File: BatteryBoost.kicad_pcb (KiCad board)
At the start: 2 copper layers, 78 x 40 mm, 35 parts, among them J1 USB_B_Micro, J2 Conn_01x02, J3 Conn_01x02, J4 Mounting Hole, J5 Mounting Hole, J6 Mounting Hole, J7 Mounting Hole, Q1 Q_PMOS_GSD, SW1 SW_SPDT, U1 SP34063AEN, U2 TP4056

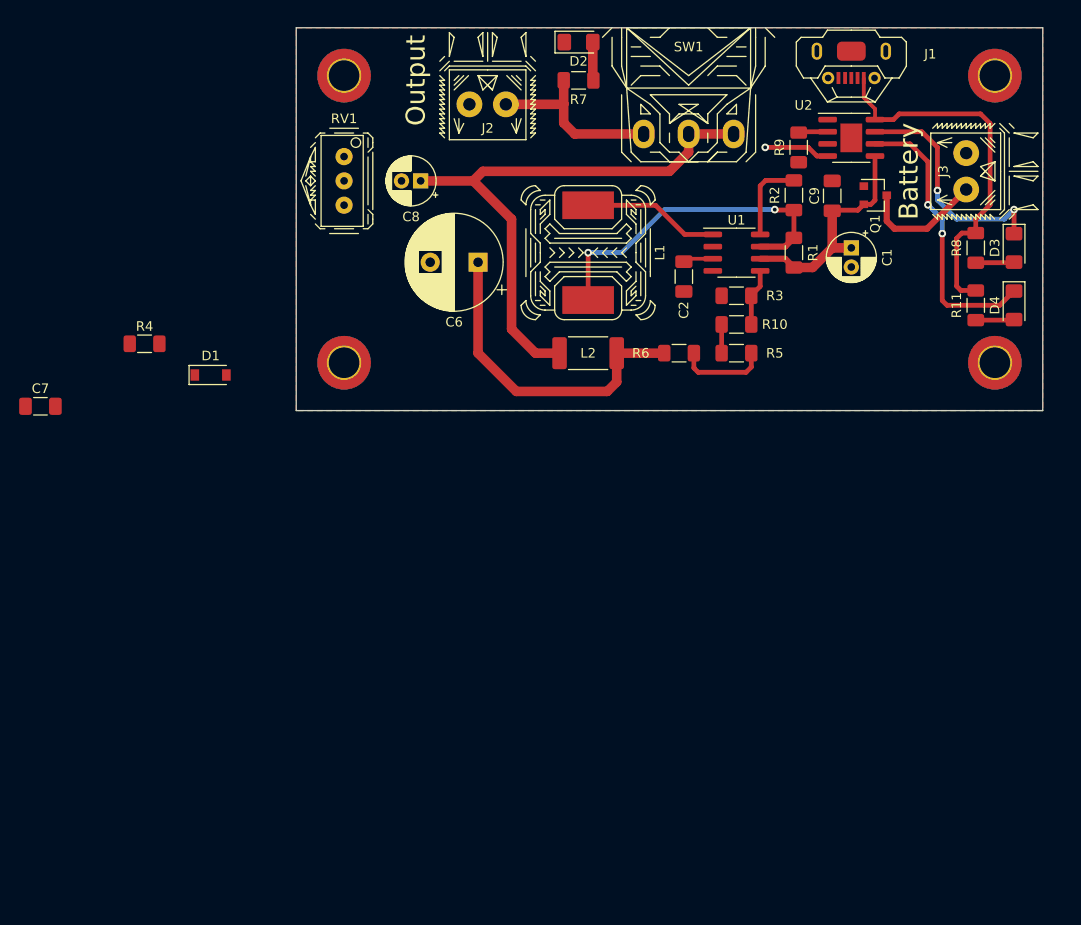
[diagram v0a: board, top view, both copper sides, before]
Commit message: add chamfer to board edge
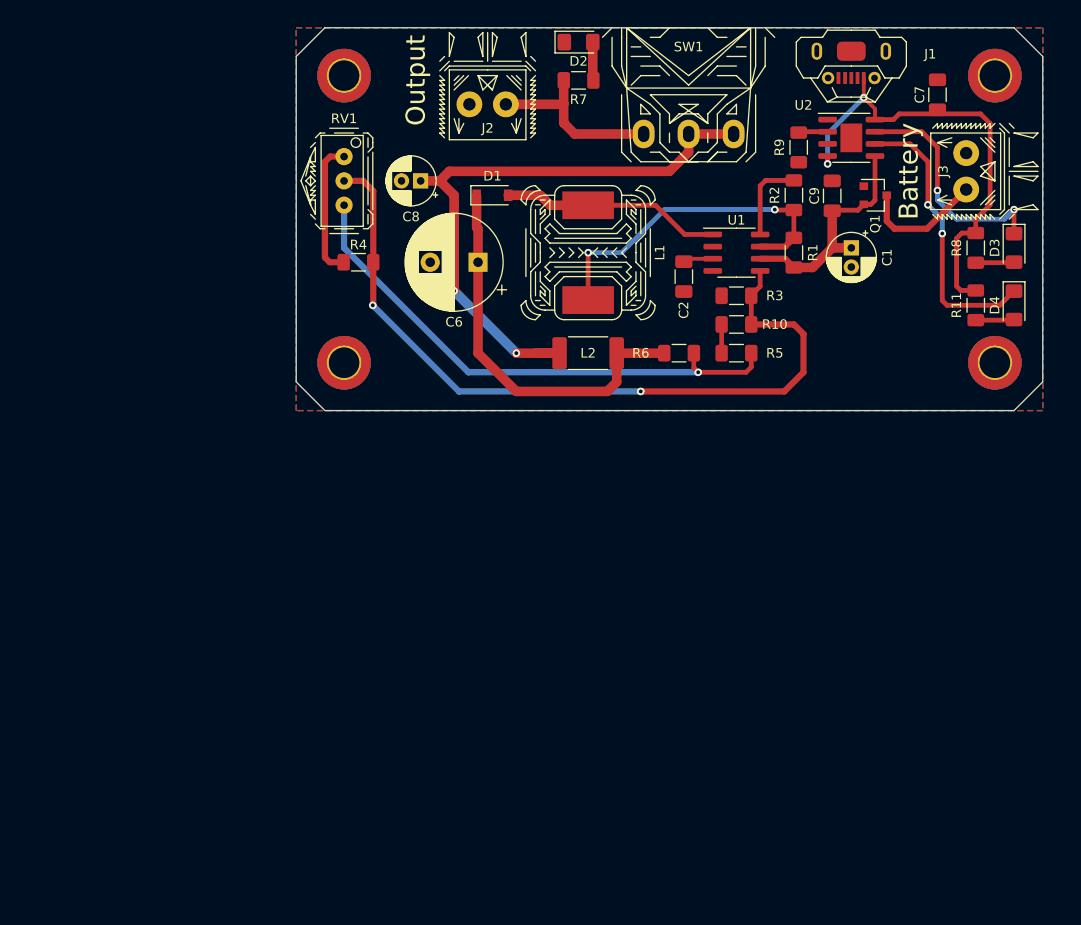
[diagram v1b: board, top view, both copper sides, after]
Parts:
- moved C7 99.2 mm to (67.0, 7.00), turned to 90 degrees
- moved D1 34.9 mm to (20.5, 17.5)
- moved R4 23.9 mm to (6.50, 24.5)
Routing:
- net Net-(R10-Pad2): track 5.98 -> 80.9 mm, vias 0 -> 2
- net Net-(R5-Pad1): track 9.41 -> 56.3 mm, vias 0 -> 1
- net Net-(R4-Pad1): track 0.00 -> 14.4 mm
- net Net-(D1-Pad2): track 14.3 -> 23.1 mm
- net Net-(C6-Pad1): track 34.1 -> 41.2 mm
- net +24V: track 59.0 -> 64.2 mm, vias 0 -> 2
- net +5V: track 45.9 -> 48.3 mm, vias 1 -> 2
- added copper zone on B.Cu, net GND
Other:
- outline, holes or cut-outs redrawn

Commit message: finalize designs
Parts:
- added D5: 40V 1A 450mV @ 1A, Diode_SMD:D_SOD-123, F.Cu at (58.0, 23.5)
- added D6: 40V 1A 450mV @ 1A, Diode_SMD:D_SOD-123, F.Cu at (55.0, 23.5)
- added G***: LOGO, BatteryBoost:F_Artwork, F.Cu at (40.0, 20.0)
- D1: value 40V 1A 450mV @ 1A -> 600V 5A 1.2V; footprint Diode_SMD:D_SOD-123 -> Diode_SMD:D_SMB
- L1: footprint BatteryBoost:Inductor_SLH_12x12x8 -> BatteryBoost:Inductor_SLH_12x12x8_HandSolder
- moved L2 20.9 mm to (42.2, 16.8)
- moved C1 4.91 mm to (62.8, 24.2), turned to 0 degrees
- moved D1 1.80 mm to (19.9, 15.8)
- moved J1 0.25 mm to (58.0, 5.00)
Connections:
- C1 pad 1: VBATT -> Net-(C1-Pad1)
- R1 pad 2: VBATT -> Net-(C1-Pad1)
- U1 pad 2: Net-(U1-Pad2) -> GND
- U1 pad 6: VBATT -> Net-(C1-Pad1)
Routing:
- net Net-(C6-Pad1): track 41.2 -> 67.2 mm, vias 0 -> 2
- net +24V: track 64.2 -> 40.9 mm, vias 2 -> 0
- net Net-(C1-Pad1): track 0.00 -> 15.1 mm
- net Net-(D1-Pad2): track 23.1 -> 9.63 mm
- net VBATT: track 24.2 -> 12.7 mm
- net +5V: track 48.3 -> 57.4 mm, vias 2 -> 3
- net Net-(R10-Pad2): track 80.9 -> 75.4 mm
- added copper zone on F.Cu, net Net-(D1-Pad2)
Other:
- board text removed: "Battery"
- board text removed: "Output"

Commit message: Finalize schematic and layout
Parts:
- removed D5, D6: 40V 1A 450mV @ 1A, Diode_SMD:D_SOD-123
- removed G***: LOGO, BatteryBoost:F_Artwork
- added Q2: Q_PMOS_GSD, Package_TO_SOT_SMD:SOT-23, F.Cu at (56.5, 23.8)
- added Q3: Q_PMOS_GSD, Package_TO_SOT_SMD:SOT-23, F.Cu at (62.0, 23.8)
- added R12: 1M, Resistor_SMD:R_1206_3216Metric_Pad1.30x1.75mm_HandSolder, F.Cu at (57.5, 35.5)
- added R14: 10k, Resistor_SMD:R_1206_3216Metric_Pad1.30x1.75mm_HandSolder, F.Cu at (64.8, 35.5)
- added U3: SN74LVC2G04DBVR, Package_TO_SOT_SMD:SOT-23-6, F.Cu at (61.0, 31.0)
- J2: value Conn_01x02 -> Output
- J3: value Conn_01x02 -> Battery
- Q1: footprint Package_TO_SOT_SMD:SC-59 -> Package_TO_SOT_SMD:SOT-23
- moved L2 13.4 mm to (29.5, 12.8)
- moved C1 8.40 mm to (55.0, 27.5), turned to 270 degrees
- moved R7 2.50 mm to (29.5, 8.00)
- moved D2 2.00 mm to (29.5, 3.50)
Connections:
- J2 pad 1: Net-(J2-Pad1) -> +24V
- R7 pad 1: Net-(J2-Pad1) -> +24V
- SW1 pad 1: Net-(J2-Pad1) -> Net-(C1-Pad1)
- SW1 pad 2: +24V -> SMPS_Pwr
- SW1 pad 3: +24V -> Net-(SW1-Pad3)
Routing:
- net VBATT: track 12.7 -> 50.3 mm, vias 0 -> 2
- net SMPS_Pwr: track 0.00 -> 31.0 mm, vias 0 -> 2
- net Net-(J2-Pad1): track 19.3 -> 0.00 mm
- net Net-(C1-Pad1): track 15.1 -> 31.9 mm
- net Net-(Q3-Pad1): track 0.00 -> 15.1 mm
- net +5V: track 57.4 -> 72.0 mm, vias 3 -> 4
- net +24V: track 40.9 -> 27.0 mm
- net Net-(C6-Pad1): track 67.2 -> 59.8 mm
- net GND: track 0.00 -> 6.04 mm, vias 0 -> 7
- net Net-(L1-Pad2): track 35.1 -> 34.5 mm
- net Net-(D2-Pad2): track 4.03 -> 4.53 mm

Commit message: A01 Release Files
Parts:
- removed the Q2 at (56.5, 23.8)
- added G***: LOGO, BatteryBoost:B_Artwork, B.Cu at (39.0, 20.0)
- added G***: LOGO, BatteryBoost:F_Artwork, F.Cu at (39.0, 20.0)
- added Q1: Q_PMOS_GSD, Package_TO_SOT_SMD:SOT-23, F.Cu at (56.5, 23.8)
- L2: value 1uH ±20% 3.29A 59mΩ SMD,2.5x2x1.2mm -> 1uH ±20% 3.29A 59mΩ
- R1: value 0.22 R -> 0.3R
- renumbered C7 to C2, C2 to C3, C6 to C4, C9 to C5, C8 to C6, D4 to D1, D1 to D2, D2 to D4, J4 to J1, J5 to J2, J6 to J3, J7 to J4, J1 to J5, J3 to J6, J2 to J7, Q1 to Q2, R12 to R10, R9 to R11, R7 to R12, R14 to R13, R10 to R3, R3 to R4, R11 to R5, R5 to R6, R4 to R7, R6 to R9
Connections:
- U2 pad 9: (no net) -> GND
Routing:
- net GND: track 6.04 -> 9.33 mm, vias 7 -> 8
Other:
- board text added: "JLCJLCJLCJLC"

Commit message: Clear board
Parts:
- removed C1, C6: 100uF ±20% 50V, Capacitor_THT:CP_Radial_D5.0mm_P2.00mm
- removed C2, C5: 10uF, Capacitor_SMD:C_1206_3216Metric_Pad1.33x1.80mm_HandSolder
- removed C3: 1.5nF ±10% 50V X7R 1206, Capacitor_SMD:C_1206_3216Metric_Pad1.33x1.80mm_HandSolder
- removed C4: 330uF ±20% 50V, Capacitor_THT:CP_Radial_D10.0mm_P5.00mm
- removed D1, D4: Blue LED, Diode_SMD:D_1206_3216Metric_Pad1.42x1.75mm_HandSolder
- removed D2: 600V 5A 1.2V, Diode_SMD:D_SMB
- removed D3: Red LED, Diode_SMD:D_1206_3216Metric_Pad1.42x1.75mm_HandSolder
- removed G***: LOGO, BatteryBoost:B_Artwork
- removed G***: LOGO, BatteryBoost:F_Artwork
- removed J5: USB_B_Micro, BatteryBoost:U-F-M5DD-Y-L
- removed J6: Battery, BatteryBoost:WJ124-3.81-2P
- removed J7: Output, BatteryBoost:WJ124-3.81-2P
- removed L1: 150uH ±20% 1.42A 280mΩ, BatteryBoost:Inductor_SLH_12x12x8_HandSolder
- removed L2: 1uH ±20% 3.29A 59mΩ, Inductor_SMD:L_2512_6332Metric_Pad1.52x3.35mm_HandSolder
- removed Q1, Q2, Q3: Q_PMOS_GSD, Package_TO_SOT_SMD:SOT-23
- removed R1: 0.3R, Resistor_SMD:R_1206_3216Metric_Pad1.30x1.75mm_HandSolder
- removed R10: 1M, Resistor_SMD:R_1206_3216Metric_Pad1.30x1.75mm_HandSolder
- removed R11: 1.2 k, Resistor_SMD:R_1206_3216Metric_Pad1.30x1.75mm_HandSolder
- removed R12, R13, R5, R8: 10k, Resistor_SMD:R_1206_3216Metric_Pad1.30x1.75mm_HandSolder
- removed R2: 180R, Resistor_SMD:R_1206_3216Metric_Pad1.30x1.75mm_HandSolder
- removed R3: 499k 0.25W 1%, Resistor_SMD:R_1206_3216Metric_Pad1.30x1.75mm_HandSolder
- removed R4: 16k, Resistor_SMD:R_1206_3216Metric_Pad1.30x1.75mm_HandSolder
- removed R6: 9.1k 1% 0.25W, Resistor_SMD:R_1206_3216Metric_Pad1.30x1.75mm_HandSolder
- removed R7: 0R, Resistor_SMD:R_1206_3216Metric_Pad1.30x1.75mm_HandSolder
- removed R9: 48k, Resistor_SMD:R_1206_3216Metric_Pad1.30x1.75mm_HandSolder
- removed RV1: 500k, BatteryBoost:Potentiometer_3296W-1-504
- removed SW1: SW_SPDT, BatteryBoost:Switch_SS-12D06L5
- removed U1: SP34063AEN, Package_SO:SOIC-8_3.9x4.9mm_P1.27mm
- removed U2: TP4056, BatteryBoost:SOIC-8-1EP_3.9x4.9mm_P1.27mm_EP2.29x3mm
- removed U3: SN74LVC2G04DBVR, Package_TO_SOT_SMD:SOT-23-6
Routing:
- net Net-(R3-Pad2): track 75.4 -> 0.00 mm, vias 2 -> 0
- net +5V: track 72.0 -> 0.00 mm, vias 4 -> 0
- net Net-(C4-Pad1): track 59.8 -> 0.00 mm, vias 2 -> 0
- net Net-(R6-Pad1): track 56.3 -> 0.00 mm, vias 1 -> 0
- net VBATT: track 50.3 -> 0.00 mm, vias 2 -> 0
- net Net-(L1-Pad2): track 34.5 -> 0.00 mm, vias 2 -> 0
- net Net-(C1-Pad1): track 31.9 -> 0.00 mm
- net SMPS_Pwr: track 31.0 -> 0.00 mm, vias 2 -> 0
- net Net-(D1-Pad1): track 29.7 -> 0.00 mm, vias 2 -> 0
- net +24V: track 27.0 -> 0.00 mm
- net Net-(D3-Pad1): track 24.5 -> 0.00 mm, vias 2 -> 0
- net Net-(Q3-Pad1): track 15.1 -> 0.00 mm
- net Net-(R7-Pad1): track 14.4 -> 0.00 mm
- net Net-(J6-Pad1): track 13.1 -> 0.00 mm
- net Net-(D2-Pad2): track 9.63 -> 0.00 mm
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- removed copper zone on F.Cu, net Net-(D2-Pad2)
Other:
- board text removed: "JLCJLCJLCJLC"

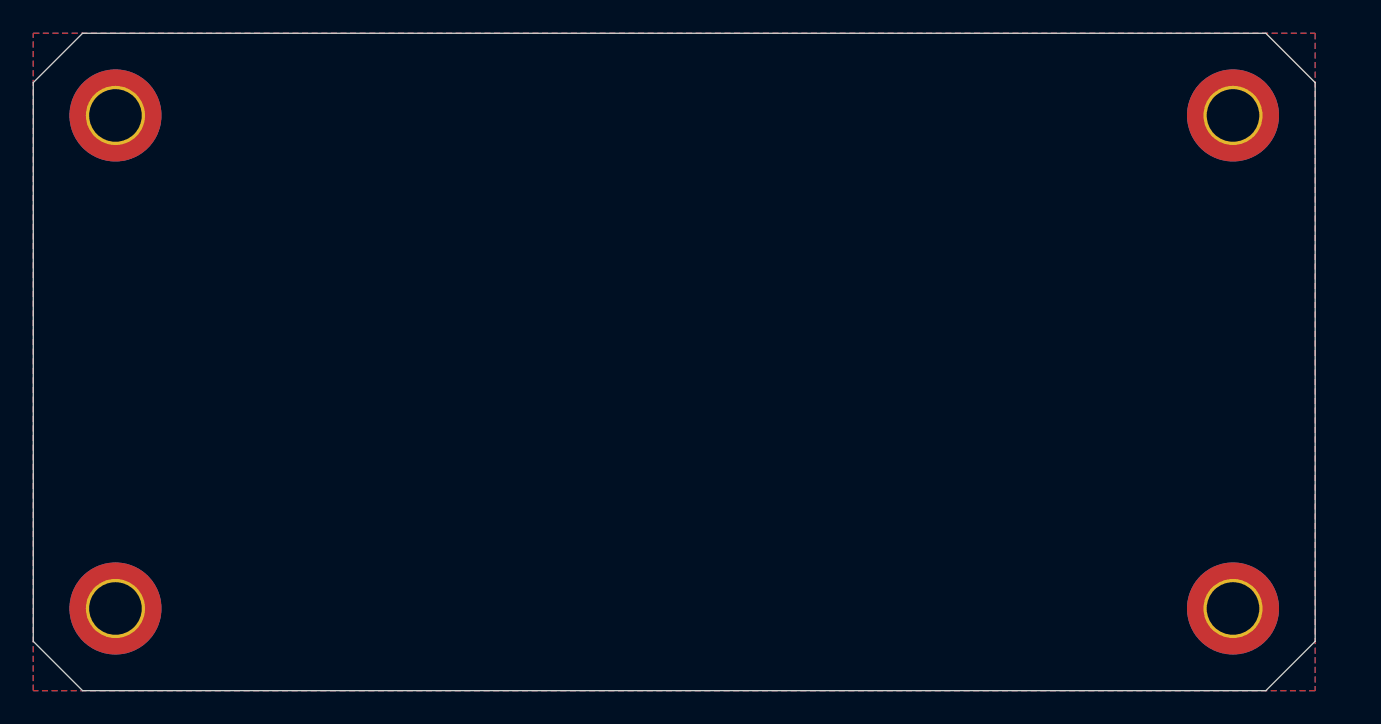
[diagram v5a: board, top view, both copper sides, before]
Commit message: update board size to 80x40mm
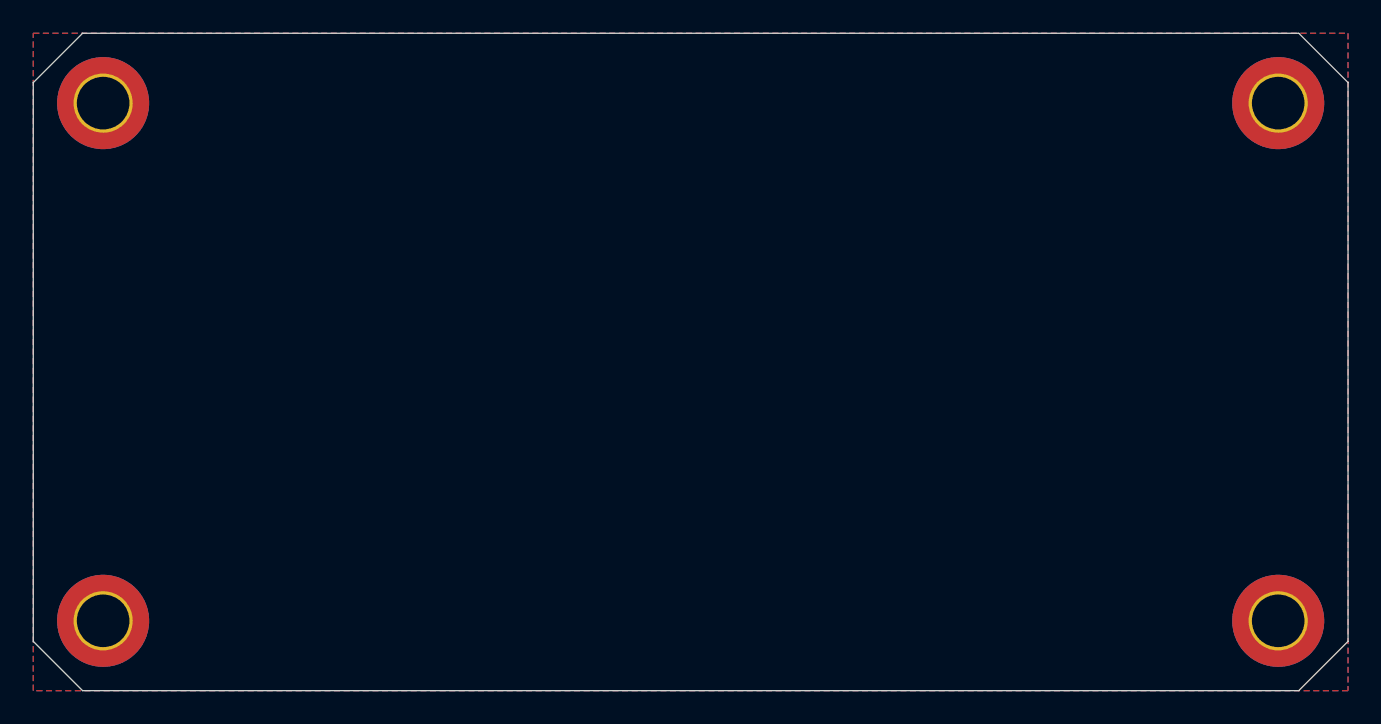
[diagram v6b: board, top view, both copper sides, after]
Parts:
- moved J2 2.85 mm to (75.8, 35.8)
- moved J3 2.85 mm to (75.8, 4.25)
- moved J1 1.06 mm to (4.25, 4.25)
- moved J4 1.06 mm to (4.25, 35.8)
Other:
- board size 78 x 40 mm -> 80 x 40 mm
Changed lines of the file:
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@@
   (general
     (thickness 1.6)
-    (drawings 8)
+    (drawings 12)
     (tracks 0)
     (zones 0)
@@
   )
   (module MountingHole:MountingHole_3.2mm_M3_DIN965_Pad_TopBottom locked (layer F.Cu)
-    (at 5 35)
+    (at 4.25 35.75)
     (descr "Mounting Hole 3.2mm, M3, DIN965")
     (tags "mounting hole 3.2mm m3 din965")
@@
   )
   (module MountingHole:MountingHole_3.2mm_M3_DIN965_Pad_TopBottom locked (layer F.Cu)
-    (at 73 5)
+    (at 75.75 4.25)
     (descr "Mounting Hole 3.2mm, M3, DIN965")
     (tags "mounting hole 3.2mm m3 din965")
@@
   )
   (module MountingHole:MountingHole_3.2mm_M3_DIN965_Pad_TopBottom locked (layer F.Cu)
-    (at 73 35)
+    (at 75.75 35.75)
     (descr "Mounting Hole 3.2mm, M3, DIN965")
     (tags "mounting hole 3.2mm m3 din965")
@@
   )
   (module MountingHole:MountingHole_3.2mm_M3_DIN965_Pad_TopBottom locked (layer F.Cu)
-    (at 5 5)
+    (at 4.25 4.25)
     (descr "Mounting Hole 3.2mm, M3, DIN965")
     (tags "mounting hole 3.2mm m3 din965")
@@
       (net 1 GND))
   )
+  (dimension 71.5 (width 0.15) (layer Dwgs.User)
+    (gr_text "71.500 mm" (at 40 -6.3) (layer Dwgs.User)
+      (effects (font (size 1 1) (thickness 0.15)))
+    )
+    (feature1 (pts (xy 75.75 -2.5) (xy 75.75 -5.586421)))
+    (feature2 (pts (xy 4.25 -2.5) (xy 4.25 -5.586421)))
+    (crossbar (pts (xy 4.25 -5) (xy 75.75 -5)))
+    (arrow1a (pts (xy 75.75 -5) (xy 74.623496 -4.413579)))
+    (arrow1b (pts (xy 75.75 -5) (xy 74.623496 -5.586421)))
+    (arrow2a (pts (xy 4.25 -5) (xy 5.376504 -4.413579)))
+    (arrow2b (pts (xy 4.25 -5) (xy 5.376504 -5.586421)))
+  )
+  (dimension 31.5 (width 0.15) (layer Dwgs.User)
+    (gr_text "31.500 mm" (at -6.3 20 90) (layer Dwgs.User)
+      (effects (font (size 1 1) (thickness 0.15)))
+    )
+    (feature1 (pts (xy -2.5 4.25) (xy -5.586421 4.25)))
+    (feature2 (pts (xy -2.5 35.75) (xy -5.586421 35.75)))
+    (crossbar (pts (xy -5 35.75) (xy -5 4.25)))
+    (arrow1a (pts (xy -5 4.25) (xy -4.413579 5.376504)))
+    (arrow1b (pts (xy -5 4.25) (xy -5.586421 5.376504)))
+    (arrow2a (pts (xy -5 35.75) (xy -4.413579 34.623496)))
+    (arrow2b (pts (xy -5 35.75) (xy -5.586421 34.623496)))
+  )
+  (dimension 80 (width 0.15) (layer Dwgs.User)
+    (gr_text "80.000 mm" (at 40 46.3) (layer Dwgs.User)
+      (effects (font (size 1 1) (thickness 0.15)))
+    )
+    (feature1 (pts (xy 80 42.5) (xy 80 45.586421)))
+    (feature2 (pts (xy 0 42.5) (xy 0 45.586421)))
+    (crossbar (pts (xy 0 45) (xy 80 45)))
+    (arrow1a (pts (xy 80 45) (xy 78.873496 45.586421)))
+    (arrow1b (pts (xy 80 45) (xy 78.873496 44.413579)))
+    (arrow2a (pts (xy 0 45) (xy 1.126504 45.586421)))
+    (arrow2b (pts (xy 0 45) (xy 1.126504 44.413579)))
+  )
+  (dimension 40 (width 0.15) (layer Dwgs.User)
+    (gr_text "40.000 mm" (at 86.3 20 270) (layer Dwgs.User)
+      (effects (font (size 1 1) (thickness 0.15)))
+    )
+    (feature1 (pts (xy 82.5 40) (xy 85.586421 40)))
+    (feature2 (pts (xy 82.5 0) (xy 85.586421 0)))
+    (crossbar (pts (xy 85 0) (xy 85 40)))
+    (arrow1a (pts (xy 85 40) (xy 84.413579 38.873496)))
+    (arrow1b (pts (xy 85 40) (xy 85.586421 38.873496)))
+    (arrow2a (pts (xy 85 0) (xy 84.413579 1.126504)))
+    (arrow2b (pts (xy 85 0) (xy 85.586421 1.126504)))
+  )
   (gr_line (start 3 40) (end 0 37) (layer Edge.Cuts) (width 0.05))
-  (gr_line (start 78 37) (end 75 40) (layer Edge.Cuts) (width 0.05))
-  (gr_line (start 75 0) (end 78 3) (layer Edge.Cuts) (width 0.05))
+  (gr_line (start 80 37) (end 77 40) (layer Edge.Cuts) (width 0.05))
+  (gr_line (start 77 0) (end 80 3) (layer Edge.Cuts) (width 0.05))
   (gr_line (start 0 3) (end 3 0) (layer Edge.Cuts) (width 0.05))
-  (gr_line (start 78 37) (end 78 3) (layer Edge.Cuts) (width 0.05))
-  (gr_line (start 3 40) (end 75 40) (layer Edge.Cuts) (width 0.05))
-  (gr_line (start 75 0) (end 3 0) (layer Edge.Cuts) (width 0.05))
+  (gr_line (start 80 37) (end 80 3) (layer Edge.Cuts) (width 0.05))
+  (gr_line (start 3 40) (end 77 40) (layer Edge.Cuts) (width 0.05))
+  (gr_line (start 77 0) (end 3 0) (layer Edge.Cuts) (width 0.05))
   (gr_line (start 0 3) (end 0 37) (layer Edge.Cuts) (width 0.05))
   (zone (net 1) (net_name GND) (layer F.Cu) (hatch edge 0.508)
@@
     (polygon
       (pts
-        (xy 78 40) (xy 0 40) (xy 0 0) (xy 78 0)
+        (xy 80 40) (xy 0 40) (xy 0 0) (xy 80 0)
       )
     )
@@
     (polygon
       (pts
-        (xy 78 40) (xy 0 40) (xy 0 0) (xy 78 0)
+        (xy 80 40) (xy 0 40) (xy 0 0) (xy 80 0)
       )
     )
